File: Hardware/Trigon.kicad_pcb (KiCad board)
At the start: 2 copper layers, 160 x 120 mm, 110 parts, among them J1 TYPE-C-31-M12_13, J2 TYPE-C-31-M12_13, J3 Conn_01x05, SW1 SW_Push, SW2 Rotary_Encoder_Switch, U1 ATmega32U4-AU, U2 USBLC6-2SC6, U3 CY7C65632-28LTXCT, U4 USBLC6-2SC6, Y1 16MHz, Y2 12MHz

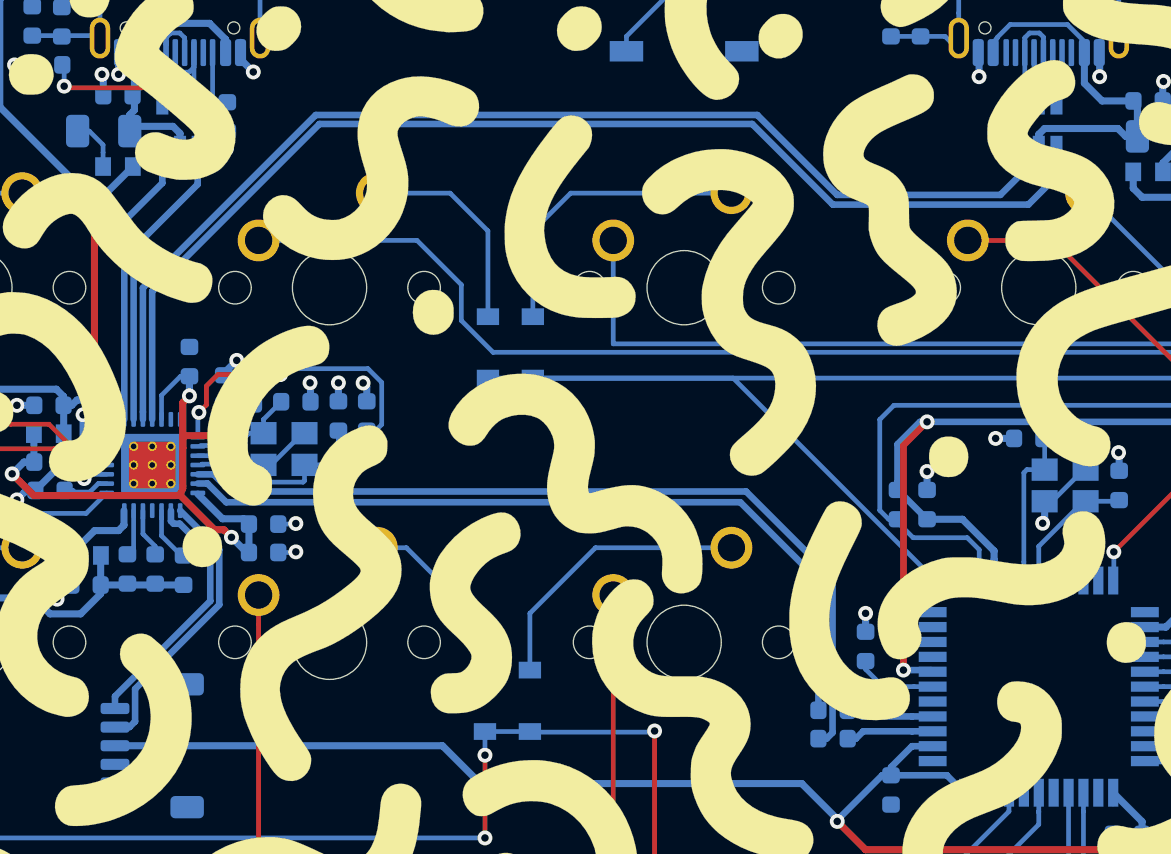
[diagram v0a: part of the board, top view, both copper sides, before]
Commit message: Addressing pcbway complaints of min track width
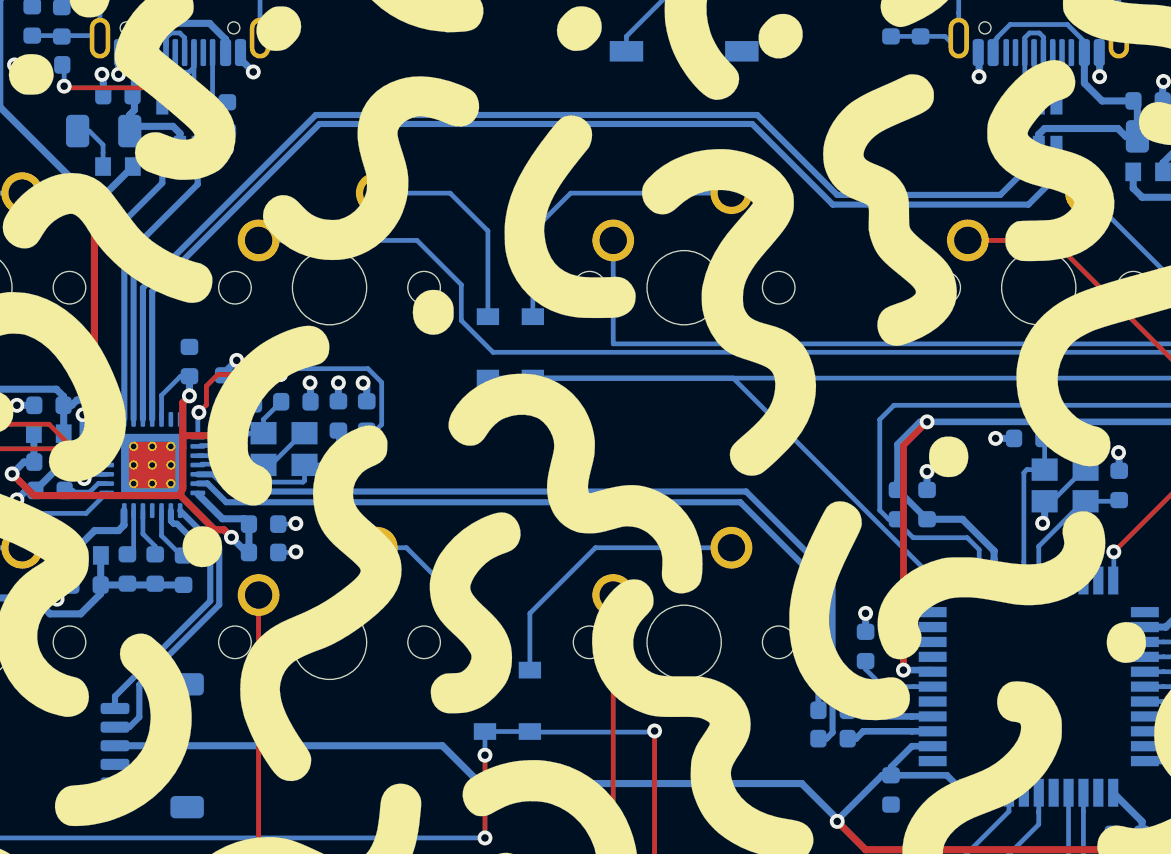
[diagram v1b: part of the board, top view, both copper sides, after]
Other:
- net class USB Differential Pair: clearance 0.127 -> 0.1524; trace_width 0.3556 -> 0.3302

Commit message: New layout
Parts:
- moved R9 14.0 mm to (92.9, 59.2), turned to 0 degrees
- moved R14 12.0 mm to (92.9, 57.7), turned to 0 degrees
- moved C12 11.8 mm to (94.2, 53.7)
- moved R13 9.89 mm to (92.9, 56.2), turned to 0 degrees
- moved FB2 6.50 mm to (95.1, 46.7), turned to 270 degrees
- moved R8 3.97 mm to (89.9, 42.5)
- moved Y2 3.87 mm to (110.1, 40.8), turned to 270 degrees
- moved C13 3.83 mm to (104.2, 39.0), turned to 0 degrees
- moved R10 3.46 mm to (108.3, 37.0), turned to 0 degrees
- moved J3 3.27 mm to (102.4, 57.9)
- moved C10 3.25 mm to (107.7, 42.3)
- moved C14 2.77 mm to (100.7, 36.6)
- moved C11 2.73 mm to (96.0, 37.5), turned to 90 degrees
- moved R7 2.20 mm to (89.9, 44.1)
- moved C17 2.13 mm to (103.1, 45.7), turned to 270 degrees
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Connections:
- C8 pad 1: VREG_3V3 -> Net-(C8-Pad1)
- FB1 pad 1: Net-(FB1-Pad1) -> VREG_3V3
- FB1 pad 2: VREG_3V3 -> Net-(C8-Pad1)
- U3 pad 21: Net-(FB1-Pad1) -> VREG_3V3
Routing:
- net +3.3VA: track 42.1 -> 76.2 mm, vias 4 -> 5
- net ROW1: track 128.9 -> 113.5 mm, vias 6 -> 0
- net +5V: track 288.7 -> 273.7 mm, vias 10 -> 11
- net Net-(R9-Pad2): track 2.97 -> 17.4 mm
- net nOVR_4: track 2.62 -> 15.3 mm
- net nOVR_3: track 2.71 -> 14.0 mm
- net Net-(R10-Pad1): track 16.2 -> 7.37 mm
- net Net-(C9-Pad1): track 6.11 -> 11.9 mm
- net Net-(FB1-Pad1): track 4.34 -> 0.00 mm
- net Net-(R8-Pad1): track 2.48 -> 6.62 mm
- net Net-(R3-Pad2): track 93.0 -> 89.2 mm
- net VREG_3V3: track 39.2 -> 42.8 mm, vias 2 -> 0
- net D3_D+: track 42.6 -> 45.4 mm
- net Net-(R7-Pad1): track 9.30 -> 6.58 mm
- net nOVR_2: track 8.82 -> 6.77 mm, vias 2 -> 0
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
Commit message: Latest bom/gerbers; reflecting more of josh's comments
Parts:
- moved D17 17.8 mm to (81.4, 73.9)
- moved D26 15.4 mm to (119.5, 73.8)
- moved C12 4.70 mm to (94.2, 49.0), turned to 180 degrees
- moved R3 3.75 mm to (143.0, 44.3)
- moved C6 3.62 mm to (144.5, 44.3)
- moved C4 1.51 mm to (154.6, 49.9)
- moved D16 1.18 mm to (79.0, 73.9)
- moved D18 1.17 mm to (117.1, 73.8)
- moved C3 1.17 mm to (137.3, 53.0)
- moved C7 0.73 mm to (139.2, 60.2)
- moved J3 0.54 mm to (102.0, 58.3), turned to 180 degrees
- moved C5 0.32 mm to (151.6, 61.6), turned to 0 degrees
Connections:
- J3 pad 1: D2_D+ -> GND
- J3 pad 2: D2_D- -> Net-(J3-Pad2)
- J3 pad 4: Net-(J3-Pad4) -> D2_D-
- J3 pad 5: GND -> D2_D+
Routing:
- net Net-(D26-Pad2): track 6.53 -> 21.7 mm
- net ROW0: track 307.1 -> 293.2 mm
- net GND: track 47.6 -> 52.5 mm, vias 37 -> 42
- net Net-(D17-Pad2): track 12.3 -> 16.7 mm
- net Net-(D3-Pad2): track 9.00 -> 11.5 mm
- net Net-(R3-Pad2): track 89.2 -> 86.7 mm
- net +5V: track 273.7 -> 276.1 mm
- net Net-(D4-Pad2): track 14.6 -> 16.6 mm
- net Net-(D11-Pad2): track 14.6 -> 16.6 mm
- net +3.3VA: track 76.2 -> 78.0 mm
- net D2_D-: track 13.6 -> 11.9 mm
- net Net-(D10-Pad2): track 9.94 -> 11.5 mm
- net D2_D+: track 13.4 -> 11.9 mm
- net Net-(C3-Pad1): track 4.43 -> 3.60 mm
- net ROW1: track 113.5 -> 114.2 mm
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
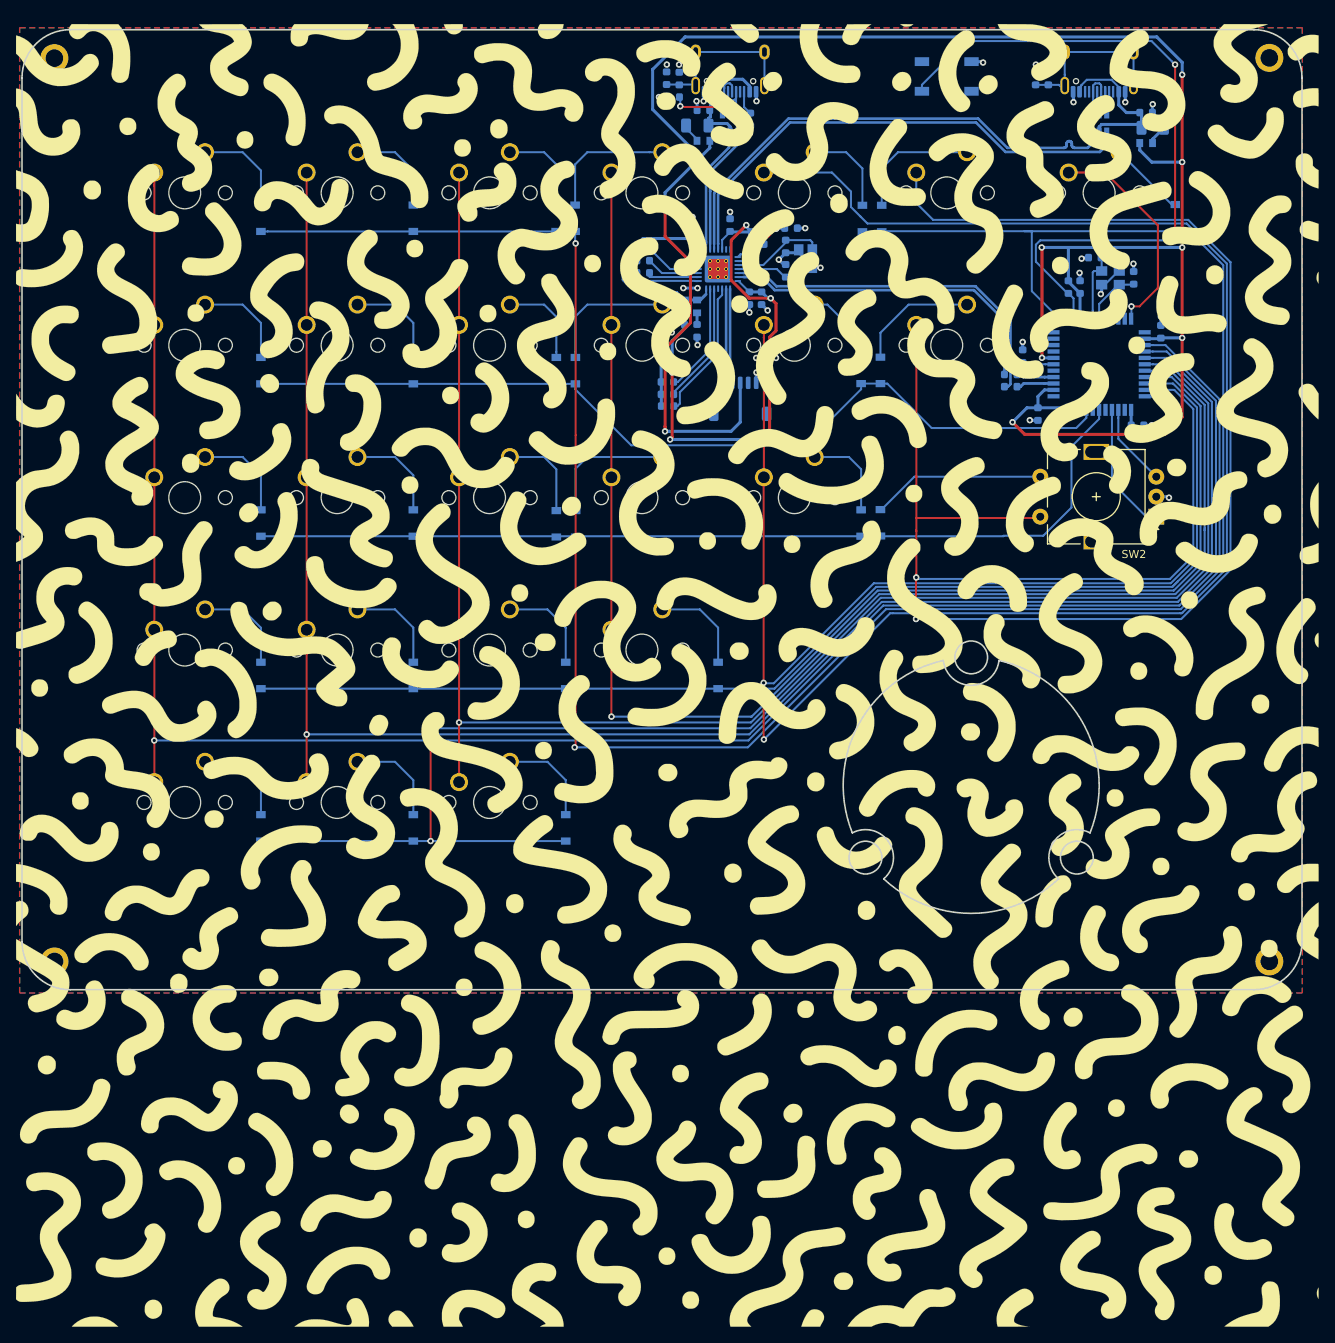
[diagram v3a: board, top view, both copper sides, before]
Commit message: Updates to case
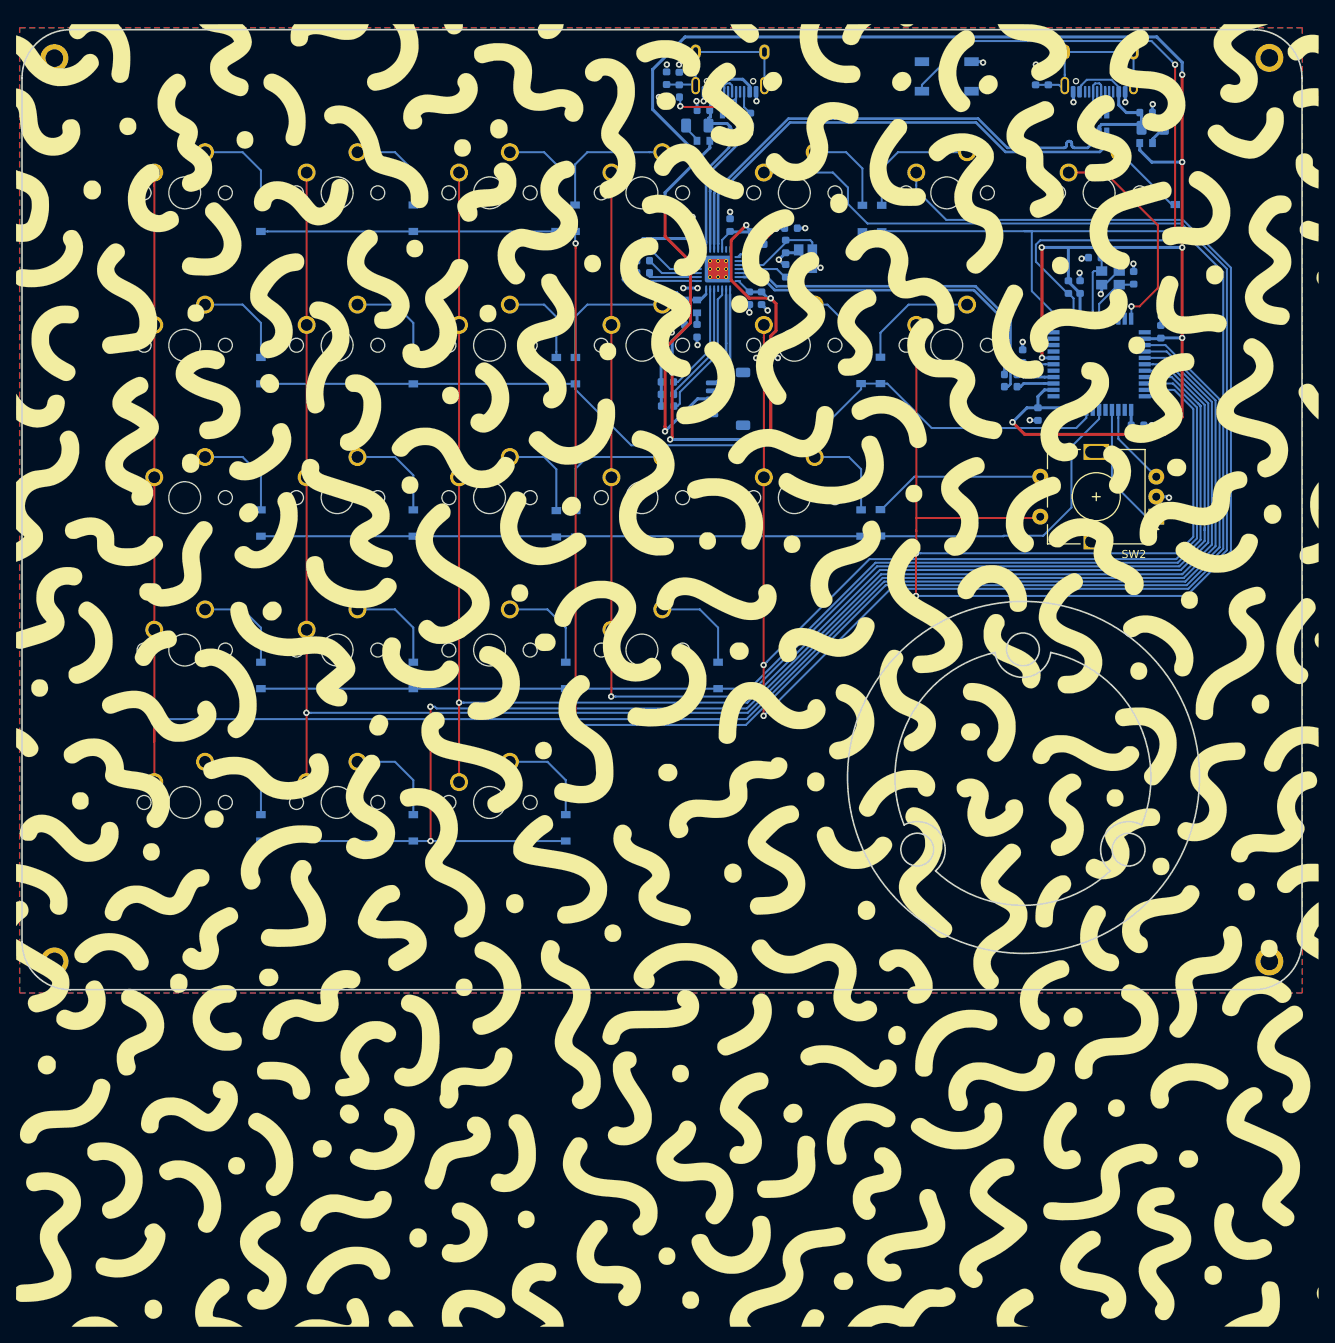
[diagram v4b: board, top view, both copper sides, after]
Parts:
- moved J3 1.52 mm to (100.5, 58.3), turned to 270 degrees
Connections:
- J3 pad 1: GND -> D2_D+
- J3 pad 2: Net-(J3-Pad2) -> D2_D-
- J3 pad 4: D2_D- -> Net-(J3-Pad4)
- J3 pad 5: D2_D+ -> GND
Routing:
- net COL5: track 241.9 -> 231.9 mm
- net COL4: track 308.8 -> 300.4 mm
- net +5V: track 276.1 -> 268.8 mm
- net ROW0: track 293.2 -> 287.2 mm
- net COL3: track 179.3 -> 174.3 mm
- net COL1: track 230.5 -> 228.1 mm
- net D2_D+: track 11.9 -> 14.2 mm
- net D2_D-: track 11.9 -> 14.2 mm
- net ROW3: track 152.7 -> 150.8 mm
- net GND: track 52.5 -> 51.4 mm, vias 42 -> 41
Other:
- outline, holes or cut-outs redrawn
- board text added: "rev 0.1.1"
- board text removed: "rev 0.1"

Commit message: checkpoint
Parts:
- MH1, MH2, MH3, MH4: footprint random-keyboard-parts:Generic-Mounthole -> CustomMounting:MountingHole_3.2mm_M3_Pad_v2
- moved R6 37.5 mm to (123.6, 78.6), turned to 0 degrees
- moved C4 35.9 mm to (132.7, 78.4), turned to 0 degrees
- moved C1 34.2 mm to (138.6, 75.0), turned to 0 degrees
- moved C5 33.6 mm to (121.0, 75.4), turned to 270 degrees
- moved Y1 30.5 mm to (138.6, 72.1), turned to 90 degrees
- moved C2 29.9 mm to (141.1, 70.1), turned to 90 degrees
- moved D26 29.4 mm to (146.1, 61.1), turned to 270 degrees
- moved SW1 28.8 mm to (156.6, 16.7)
- moved C6 24.9 mm to (137.4, 68.3), turned to 0 degrees
- moved U1 24.7 mm to (128.6, 70.6), turned to 270 degrees
- moved R3 23.2 mm to (137.4, 66.8), turned to 180 degrees
- moved D7 19.1 mm to (137.3, 35.7)
- moved D13 17.8 mm to (137.3, 54.7)
- moved C7 17.1 mm to (122.4, 63.0), turned to 180 degrees
- moved D18 16.6 mm to (100.5, 73.8)
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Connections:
- D13 pad 1: ROW1 -> ROW1.5
- D26 pad 1: ROW2 -> ROW1.5
- D5 pad 1: ROW0 -> ROW0.5
- D6 pad 1: ROW0 -> ROW0.5
- D7 pad 1: ROW0 -> ROW0.5
- MX5 pad 1: COL4 -> COL3.5
- SW2 pad A: ENC1B -> ENC1A
- SW2 pad B: ENC1A -> ENC1B
- SW2 pad S1: Net-(D26-Pad2) -> COL6
- SW2 pad S2: COL5 -> Net-(D26-Pad2)
- U1 pad 10: Net-(U1-Pad10) -> ROW0.5
- U1 pad 11: Net-(U1-Pad11) -> ROW1.5
- U1 pad 12: ROW0 -> COL6
- U1 pad 21: Net-(U1-Pad21) -> ENC1A
- U1 pad 22: COL6 -> ENC1B
- U1 pad 25: COL0 -> ROW4
- U1 pad 26: COL1 -> ROW3
- U1 pad 27: ROW4 -> COL3
- U1 pad 29: COL3 -> COL1
- U1 pad 30: ROW3 -> COL0
- U1 pad 32: COL5 -> Net-(U1-Pad32)
- U1 pad 36: ENC1A -> Net-(U1-Pad36)
- U1 pad 37: ENC1B -> Net-(U1-Pad37)
- U1 pad 38: Net-(U1-Pad38) -> ROW0
- U1 pad 8: Net-(U1-Pad8) -> COL5
- U1 pad 9: Net-(U1-Pad9) -> COL3.5
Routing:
- net COL4: track 300.4 -> 58.0 mm, vias 2 -> 1
- net COL5: track 231.9 -> 45.5 mm, vias 2 -> 0
- net ROW0: track 287.2 -> 123.6 mm
- net ROW4: track 189.7 -> 105.6 mm, vias 2 -> 0
- net COL0: track 251.7 -> 179.8 mm
- net COL3: track 174.3 -> 105.8 mm
- net COL1: track 228.1 -> 161.4 mm
- net COL2: track 208.8 -> 143.4 mm
- net COL3.5: track 0.00 -> 57.5 mm
- net ROW3: track 150.8 -> 97.0 mm
- net ROW0.5: track 0.00 -> 51.2 mm
- net +5V: track 268.8 -> 223.4 mm, vias 11 -> 10
- net ROW2: track 116.5 -> 82.8 mm
- net Net-(D4-Pad2): track 16.6 -> 48.9 mm
- net ENC1B: track 16.4 -> 44.1 mm
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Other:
- outline, holes or cut-outs redrawn
